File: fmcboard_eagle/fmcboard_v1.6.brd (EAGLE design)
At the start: 147 x 74 mm, 292 parts, among them IC1 OPA699ID, IC10 LM358, IC11 7805DT, IC12 SN74AUC2G66DCTR, IC13 SN74AUC2G66DCTR, IC14 SN74AUC2G66DCTR, IC15 SN74AUC2G66DCTR, IC16 DAC7578SPWR, IC17 SN74AUC2G66DCTR, IC18 SN74AUC2G66DCTR, IC19 SN74AUC2G66DCTR, IC2 DAC7578SPWR, IC20 SN74AUC2G66DCTR, IC21 74AUP2GU04GW, IC22 74AUP2GU04GW, IC23 74AUP2GU04GW, IC24 74AUP2GU04GW, IC25 MC7905ACD2TR4G, IC26 AMS1117-1.8, IC27 LM358, IC28 SN74AUC2G66DCTR, IC29 LM337KVURG3, IC3 LTC6229IMS8E#TRPBF, IC30 SN74AUC2G66DCTR, IC31 SN74AUC2G66DCTR, IC32 SN74AUC2G66DCTR, IC33 LTC6229IMS8E#TRPBF, IC34 74AUP2GU04GW, IC35 74AUP2GU04GW, IC36 TPS5430DDAR, IC37 TPS5430DDAR, IC4 OPA695IDR, IC5 LTC6229IMS8E#TRPBF, IC6 OPA695IDR, IC7 OPA699ID, IC8 LM358, IC9 LM358, J1 4p-2.54, J12 4p-2.54, J13 4p-2.54, J2 ASP-134604-01, J5 4p-2.54, J8 4p-2.54

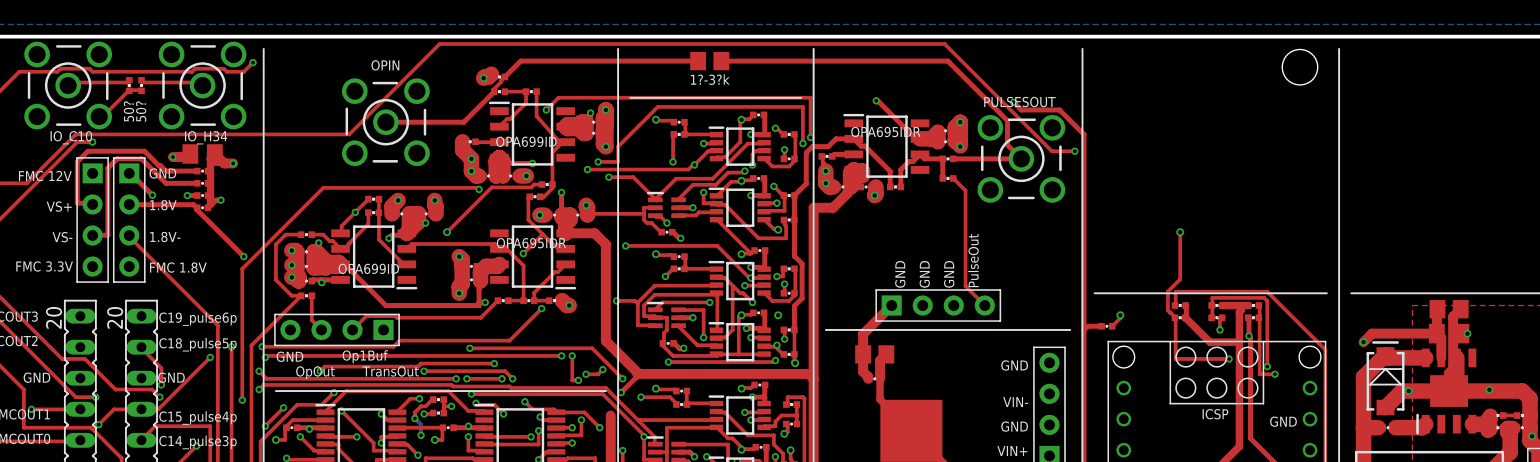
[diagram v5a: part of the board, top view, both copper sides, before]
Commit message: add buffered opout and pulseout smas
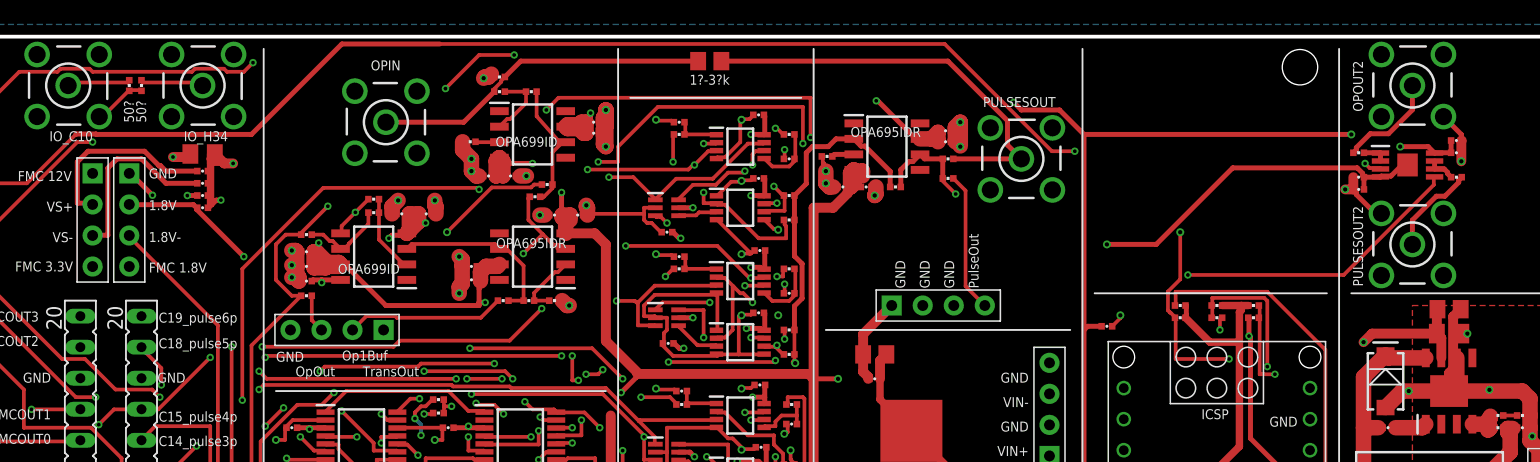
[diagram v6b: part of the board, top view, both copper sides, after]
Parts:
- added C114, C115: 100pF, passives:0402_CAP
- added C65, C86: 0.1uF, passives:0402_CAP
- added IC38: LTC6229IMS8E#TRPBF, LTC6229IMS8E#TRPBF:SOP65P490X110-9N
- added OPOUT2, PULSESOUT2: BU-SMB-V, con-coax:BU-SMB-V
- added R119, R120: 47, passives:0402_RES
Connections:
- new net N$29: IC38.1, IC38.2, R119.1
- new net N$39: PULSESOUT2.1, R120.1
- new net N$55: OPOUT2.1, R119.2
- new net N$59: IC38.6, IC38.7, R120.2
- net GND: now also C114.2, C115.2, C65.2, C86.2, OPOUT2.2, OPOUT2.3, OPOUT2.4, OPOUT2.5, PULSESOUT2.2, PULSESOUT2.3, PULSESOUT2.4, PULSESOUT2.5
- net OPOUT_H10: now also IC38.3
- net PULSESUMOUT: now also IC38.5
- net VS+: now also C114.1, C65.1, IC38.8
- net VS-: now also C115.1, C86.1, IC38.4, IC38.9
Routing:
- net OPOUT_H10: track 78.8 -> 180.2 mm, vias 1 -> 5
- net VS-: track 244.8 -> 302.4 mm, vias 12 -> 14
- net PULSESUMOUT: track 7.11 -> 54.5 mm, vias 0 -> 2
- net VS+: track 425.7 -> 457.4 mm, vias 15 -> 17
- net GND: track 535.2 -> 545.1 mm, vias 126 -> 128
- net N$55: track 0.00 -> 8.38 mm
- net N$39: track 0.00 -> 7.58 mm
- net N$59: track 0.00 -> 2.35 mm
- net N$29: track 0.00 -> 2.02 mm

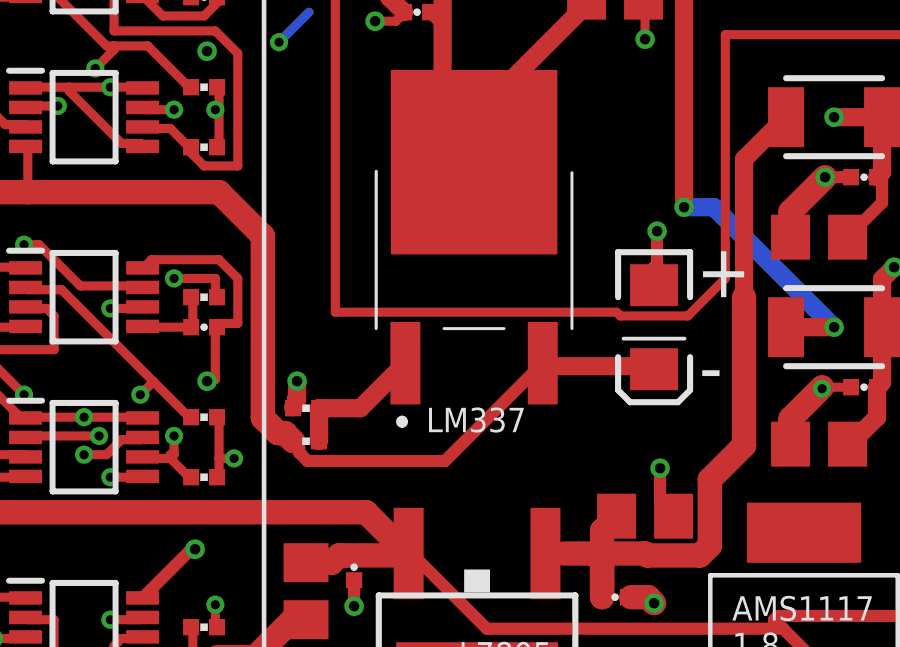
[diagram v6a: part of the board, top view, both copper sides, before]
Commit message: polarity of 2.2uF tant cap
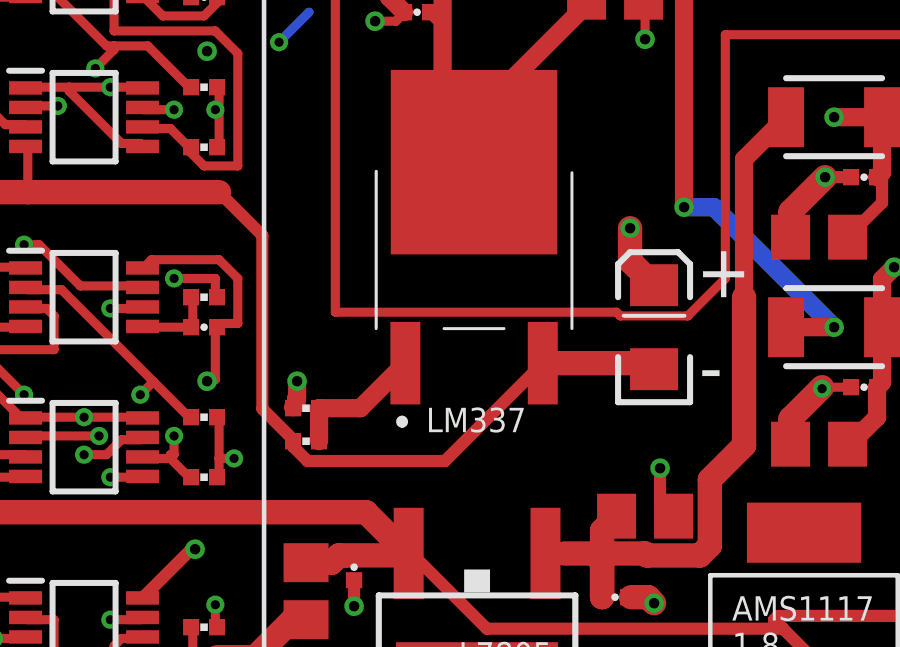
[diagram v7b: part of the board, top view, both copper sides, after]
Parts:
- turned C125 to 90 degrees
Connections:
- net 1V8-: now also C125.C; no longer C125.A
- net GND: now also C125.A; no longer C125.C
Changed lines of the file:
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@@
 <element name="R73" library="passives" package="0402_RES" value="10k" x="139" y="42" smashed="yes"/>
 <element name="R84" library="passives" package="0402_RES" value="1k" x="141" y="43" smashed="yes" rot="R180"/>
-<element name="C125" library="SparkFun-Capacitors" package="EIA3216" value="2.2uF" x="96" y="19" smashed="yes" rot="R270">
-<attribute name="LCSC" value="C122264" x="96" y="19" size="1.778" layer="27" rot="R270" display="off"/>
+<element name="C125" library="SparkFun-Capacitors" package="EIA3216" value="2.2uF" x="96" y="19" smashed="yes" rot="R90">
+<attribute name="LCSC" value="C122264" x="96" y="19" size="1.778" layer="27" rot="R90" display="off"/>
 </element>
 <element name="D2" library="SparkFun-DiscreteSemi" library_urn="urn:adsk.eagle:library:514" package="SMA-DIODE" package3d_urn="urn:adsk.eagle:package:38443/1" value="B340A" x="129.5" y="19.3" smashed="yes" rot="R90">
@@
 <contactref element="C116" pad="2"/>
 <contactref element="C117" pad="2"/>
-<contactref element="C125" pad="C"/>
 <polygon width="0.1524" layer="2" pour="cutout">
 <vertex x="55" y="14.1"/>
@@
 <via x="77.1" y="45.2" extent="1-16" drill="0.35"/>
 <via x="77.1" y="40.2" extent="1-16" drill="0.35"/>
-<via x="96.1" y="22.2" extent="1-16" drill="0.35"/>
 <via x="68.1" y="15.2" extent="1-16" drill="0.35"/>
 <via x="71.1" y="33.2" extent="1-16" drill="0.35"/>
@@
 <wire x1="61.75" y1="23" x2="61.8" y2="23.095" width="0.3048" layer="1"/>
 <wire x1="59.75" y1="21" x2="59.6047" y2="20.5" width="0.3048" layer="1"/>
-<wire x1="96" y1="22.125" x2="96.1" y2="22.2" width="0.3048" layer="1"/>
 <wire x1="98.5" y1="6" x2="98.625" y2="5.875" width="0.3048" layer="1"/>
 <wire x1="97" y1="6" x2="98.5" y2="6" width="0.3048" layer="1"/>
@@
 <wire x1="96.2" y1="14.3" x2="96.2" y2="13.15" width="0.4064" layer="1"/>
 <wire x1="96.2" y1="13.15" x2="96.65" y2="12.7" width="0.4064" layer="1"/>
-<wire x1="96" y1="21" x2="96" y2="20.4" width="0.4064" layer="1"/>
-<wire x1="96.1" y1="22.2" x2="96.1" y2="21.1" width="0.4064" layer="1"/>
-<wire x1="96.1" y1="21.1" x2="96" y2="21" width="0.4064" layer="1"/>
 <contactref element="J12" pad="1"/>
 <via x="28.9" y="61.025" extent="1-16" drill="0.3048"/>
@@
 <vertex x="127" y="61"/>
 </polygon>
+<contactref element="C125" pad="A"/>
+<via x="95.2" y="22.3" extent="1-16" drill="0.35"/>
+<wire x1="96" y1="20.4" x2="95.2" y2="21.2" width="0.8128" layer="1"/>
+<wire x1="95.2" y1="21.2" x2="95.2" y2="22.3" width="0.8128" layer="1"/>
 </signal>
 <signal name="IO1">
@@
 <contactref element="IC29" pad="3"/>
 <contactref element="R14" pad="1"/>
-<contactref element="C125" pad="A"/>
 <wire x1="92.29" y1="17.8" x2="95.7" y2="17.8" width="0.4064" layer="1"/>
-<wire x1="83.96693125" y1="15.2" x2="84.17266875" y2="14.9942625" width="0.4064" layer="1"/>
-<wire x1="84.17266875" y1="14.9942625" x2="84.17266875" y2="14.8164875" width="0.4064" layer="1"/>
-<wire x1="84.17266875" y1="14.8164875" x2="84.44955625" y2="14.5396" width="0.4064" layer="1"/>
-<wire x1="84.44955625" y1="14.5396" x2="89.0296" y2="14.5396" width="0.4064" layer="1"/>
+<wire x1="89.0296" y1="14.5396" x2="84.44955625" y2="14.5396" width="0.4064" layer="1"/>
 <wire x1="89.0296" y1="14.5396" x2="92.29" y2="17.8" width="0.4064" layer="1"/>
-<wire x1="83.96693125" y1="15.2" x2="83.69878125" y2="15.46815" width="0.8128" layer="1"/>
-<wire x1="83.69878125" y1="15.46815" x2="83.4675" y2="15.46815" width="0.8128" layer="1"/>
-<wire x1="82.9598375" y1="15.9758125" x2="82.9598375" y2="22.0401625" width="0.8128" layer="1"/>
-<wire x1="83.4675" y1="15.46815" x2="82.9598375" y2="15.9758125" width="0.8128" layer="1"/>
-<wire x1="82.9598375" y1="22.0401625" x2="81.5" y2="23.5" width="0.8128" layer="1"/>
 <wire x1="81.5" y1="23.5" x2="75.125" y2="23.5" width="0.8128" layer="1"/>
 <wire x1="75.125" y1="23.5" x2="73.375" y2="23.5" width="0.8128" layer="1"/>
@@
 <via x="60.25" y="5.625" extent="1-16" drill="0.3048"/>
 <via x="68" y="14.25" extent="1-16" drill="0.3048"/>
-<wire x1="96" y1="17.6" x2="92.49" y2="17.6" width="0.4064" layer="1"/>
 <wire x1="92.49" y1="17.6" x2="92.29" y2="17.8" width="0.4064" layer="1"/>
+<contactref element="C125" pad="C"/>
+<wire x1="92.29" y1="17.8" x2="95.8" y2="17.8" width="0.8128" layer="1"/>
+<wire x1="95.8" y1="17.8" x2="96" y2="17.6" width="0.8128" layer="1"/>
+<wire x1="84.44955625" y1="14.5396" x2="83.96693125" y2="15.022225" width="0.4064" layer="1"/>
+<wire x1="83.96693125" y1="15.022225" x2="83.96693125" y2="15.2" width="0.4064" layer="1"/>
+<wire x1="83.96693125" y1="15.2" x2="83.96693125" y2="15.2560875" width="0.4064" layer="1"/>
+<wire x1="83.96693125" y1="15.2560875" x2="82.9433625" y2="16.27965625" width="0.4064" layer="1"/>
+<wire x1="82.9433625" y1="22.0566375" x2="81.5" y2="23.5" width="0.4064" layer="1"/>
+<wire x1="82.9433625" y1="16.27965625" x2="82.9433625" y2="22.0566375" width="0.4064" layer="1"/>
 </signal>
 <signal name="N$7">
